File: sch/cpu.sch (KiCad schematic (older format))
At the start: 28 parts

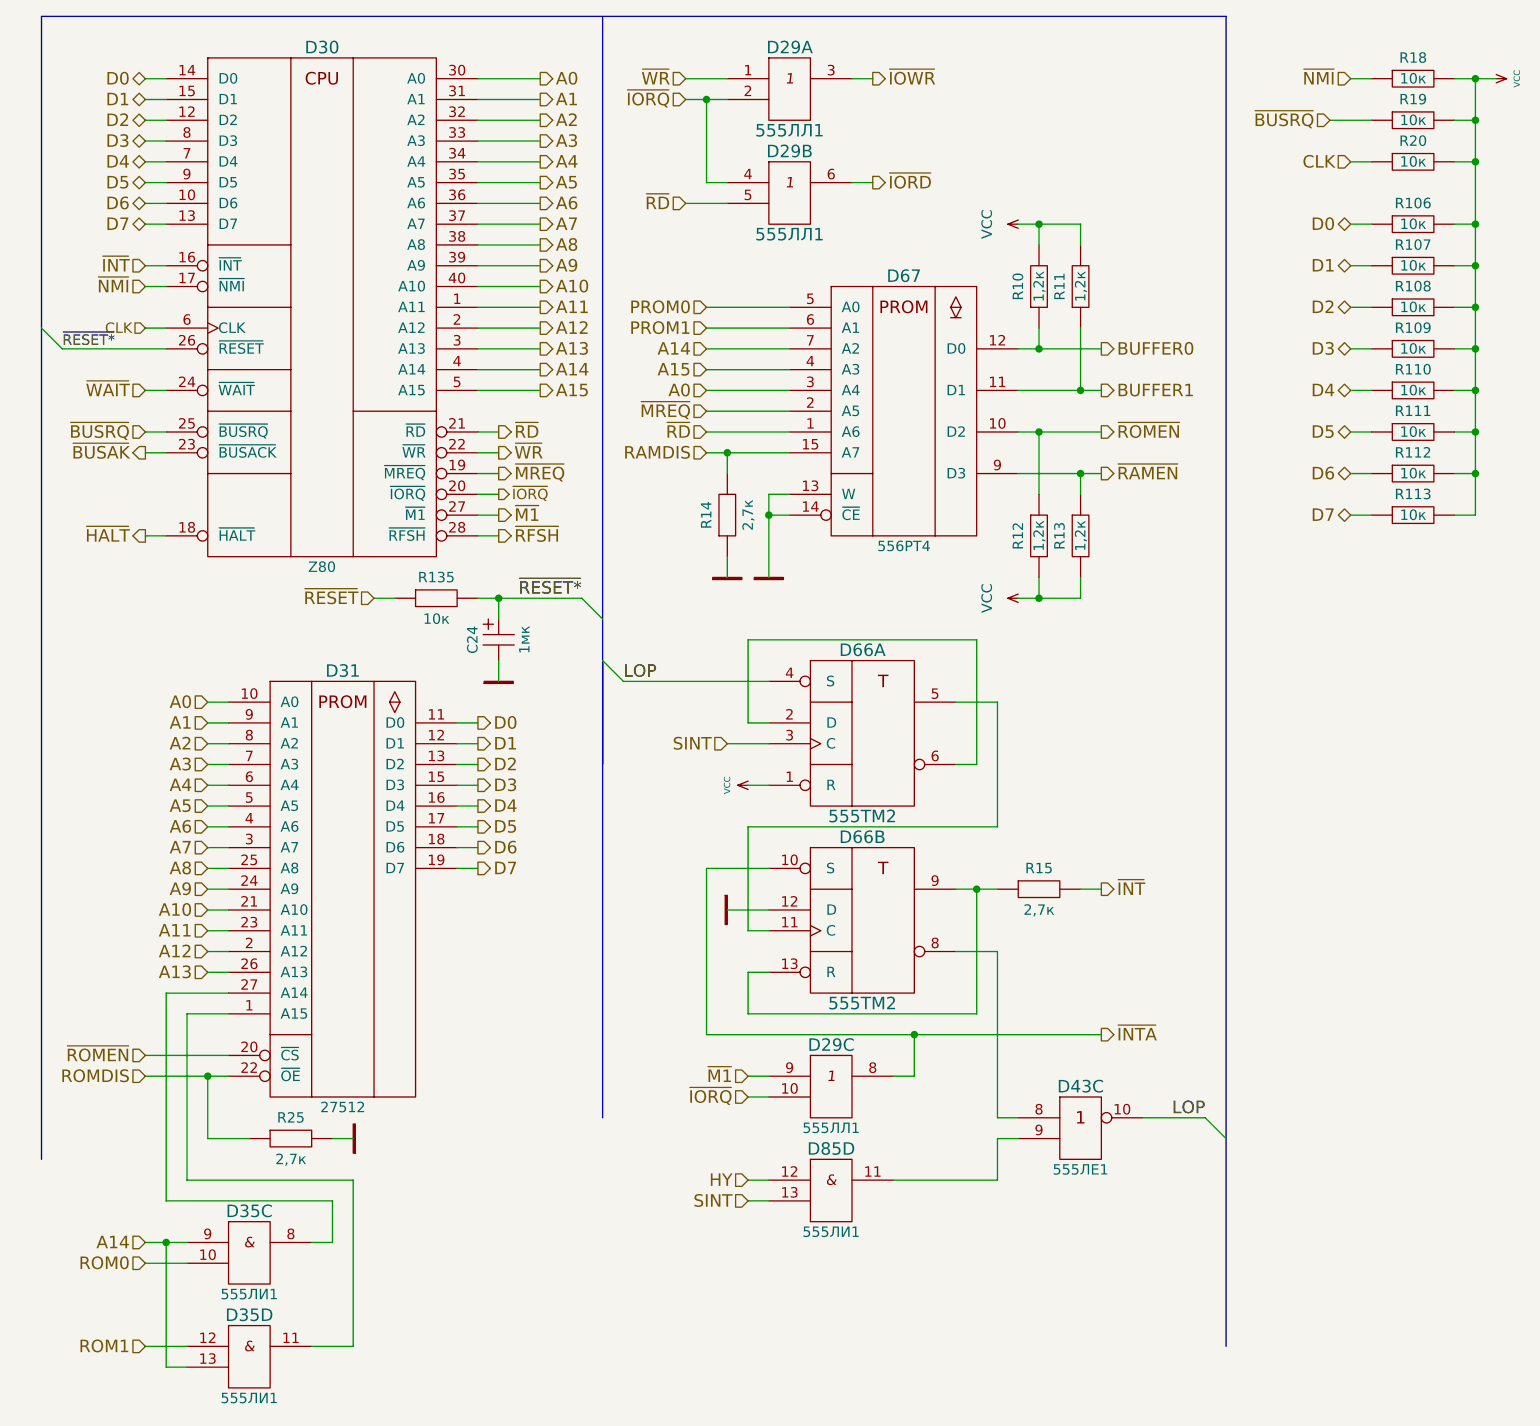
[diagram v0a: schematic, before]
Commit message: More precise version. PCB needs a lot of work.
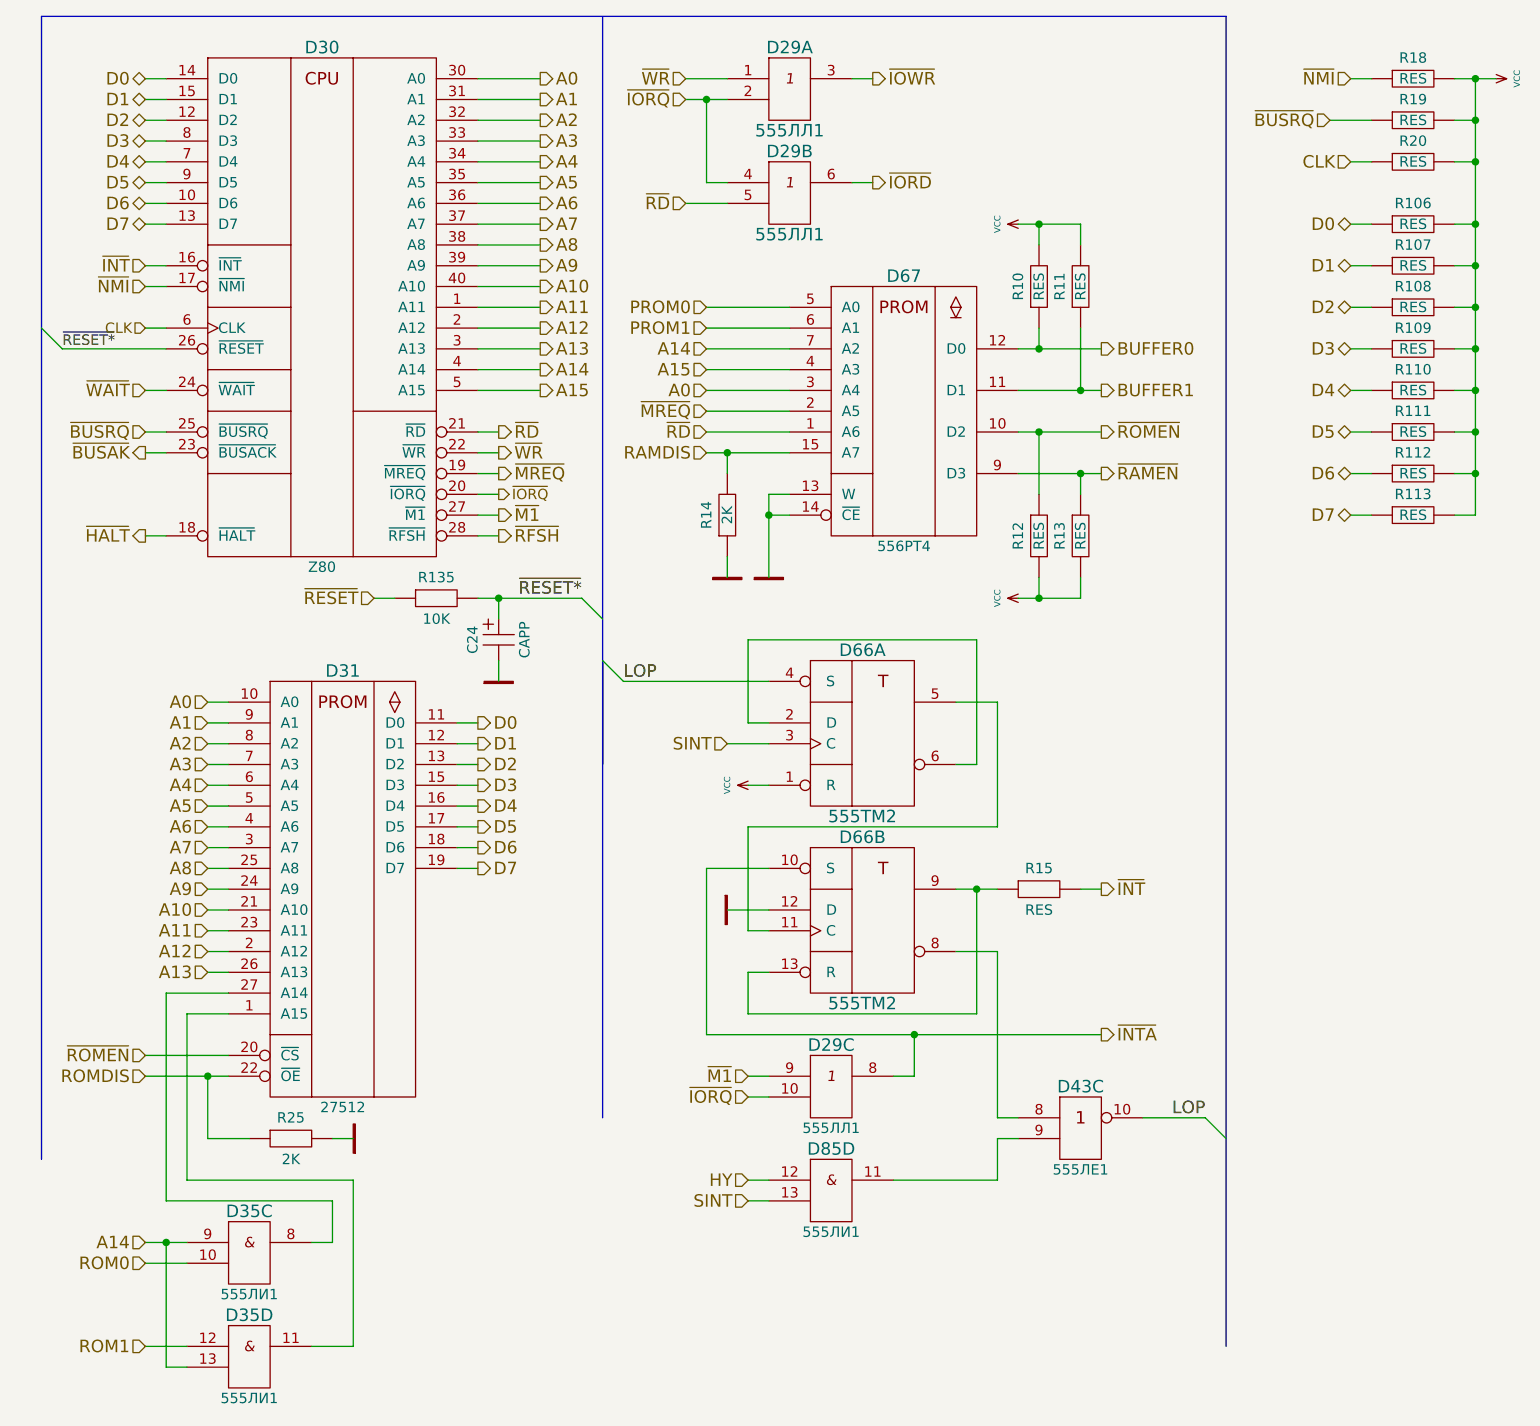
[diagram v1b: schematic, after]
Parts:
- C24: value 1мк -> CAPP
- D29, D35, D43, D66, D85: footprint MyLib:DIP-14 -> MyLib_metric:DIP-14
- D30: footprint MyLib:DIP-40 -> MyLib_metric:DIP-40
- D31: footprint MyLib:DIP-28 -> MyLib_metric:DIP-28
- D67: footprint MyLib:DIP-16 -> MyLib_metric:DIP-16
- R10, R11, R12, R13: value 1,2к -> RES; footprint MyLib:Resistor_Vertical_RM2.5mm -> MyLib_metric:Resistor_Vertical_RM2.5mm
- R106, R107, R108, R109, R110, R111, R112, R113, R18, R19, R20: value 10к -> RES; footprint MyLib:Resistor_Vertical_RM2.5mm -> MyLib_metric:Resistor_Vertical_RM2.5mm
- R135: value 10к -> 10K; footprint MyLib:Resistor_Horizontal_RM7.5mm -> MyLib_metric:Resistor_Horizontal_RM7.5mm
- R14, R25: value 2,7к -> 2K; footprint MyLib:Resistor_Horizontal_RM7.5mm -> MyLib_metric:Resistor_Horizontal_RM7.5mm
- R15: value 2,7к -> RES; footprint MyLib:Resistor_Horizontal_RM7.5mm -> MyLib_metric:Resistor_Horizontal_RM7.5mm

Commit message: IR22 and IR23 symbols updated, part values updated
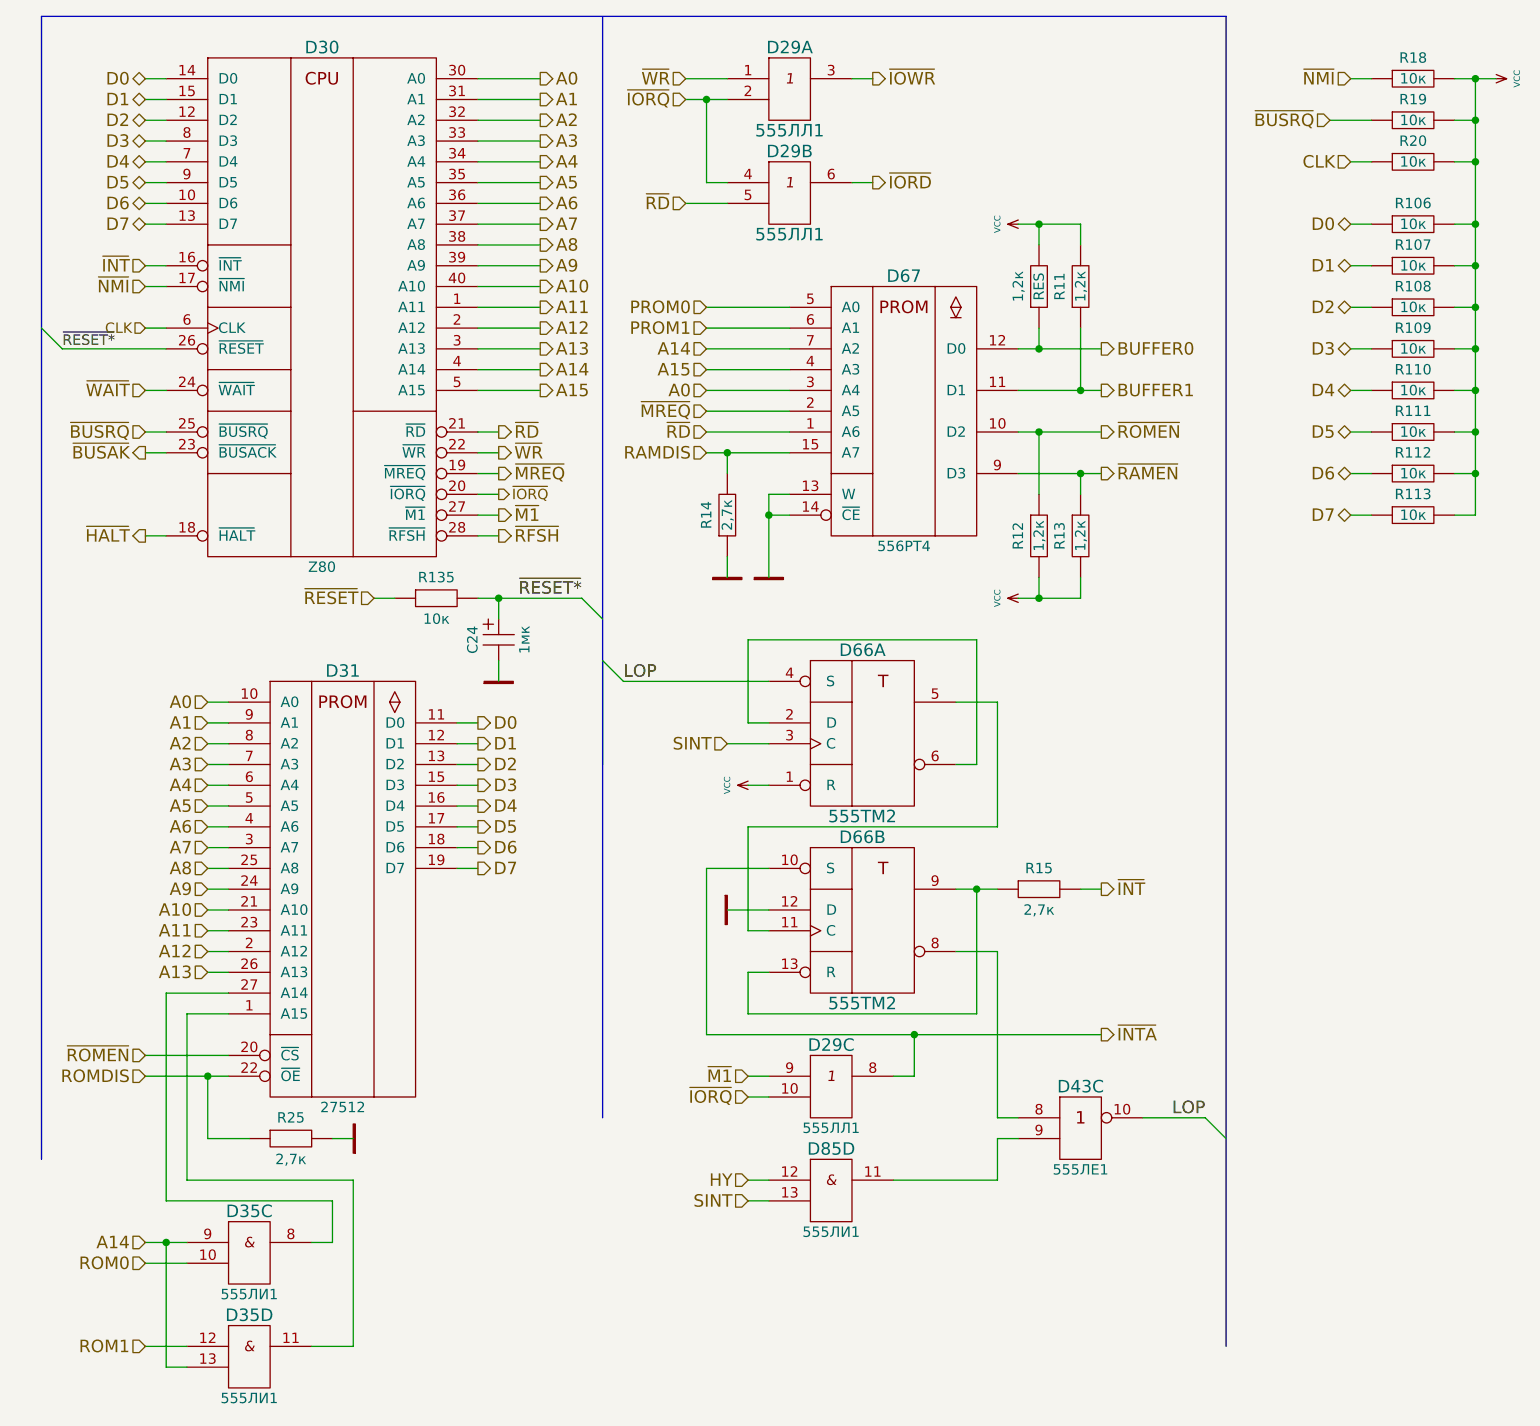
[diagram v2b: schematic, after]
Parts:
- C24: value CAPP -> 1мк
- R106, R107, R108, R109, R110, R111, R112, R113, R18, R19, R20: value RES -> 10к
- R11, R12, R13: value RES -> 1,2к
- R135: value 10K -> 10к
- R14, R25: value 2K -> 2,7к
- R15: value RES -> 2,7к
- renumbered R10 to 1,2к
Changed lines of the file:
@@
 P 1800 6000
 F 0 "R25" H 1800 6100 50  0000 C CNN
-F 1 "2K" H 1800 5900 50  0000 C CNN
+F 1 "2,7к" H 1800 5900 50  0000 C CNN
 F 2 "MyLib_metric:Resistor_Horizontal_RM7.5mm" H 1800 5950 60  0001 C CNN
 F 3 "" H 1800 5950 60  0000 C CNN
@@
 P 3900 3000
 F 0 "R14" H 3900 3100 50  0000 C CNN
-F 1 "2K" H 3900 3000 50  0000 C CNN
+F 1 "2,7к" H 3900 3000 50  0000 C CNN
 F 2 "MyLib_metric:Resistor_Horizontal_RM7.5mm" H 3900 2950 60  0001 C CNN
 F 3 "" H 3900 2950 60  0000 C CNN
@@
 	5300 2600 5700 2600
 $Comp
-L RES R10
+L RES 1,2к
 U 1 1 56901764
 P 5400 1900
-F 0 "R10" H 5400 2000 50  0000 C CNN
+F 0 "1,2к" H 5400 2000 50  0000 C CNN
 F 1 "RES" H 5400 1900 50  0000 C CNN
 F 2 "MyLib_metric:Resistor_Vertical_RM2.5mm" H 5400 1850 60  0001 C CNN
@@
 P 5600 1900
 F 0 "R11" H 5600 2000 50  0000 C CNN
-F 1 "RES" H 5600 1900 50  0000 C CNN
+F 1 "1,2к" H 5600 1900 50  0000 C CNN
 F 2 "MyLib_metric:Resistor_Vertical_RM2.5mm" H 5600 1850 60  0001 C CNN
 F 3 "" H 5600 1850 60  0000 C CNN
@@
 P 5400 3100
 F 0 "R12" H 5400 3200 50  0000 C CNN
-F 1 "RES" H 5400 3100 50  0000 C CNN
+F 1 "1,2к" H 5400 3100 50  0000 C CNN
 F 2 "MyLib_metric:Resistor_Vertical_RM2.5mm" H 5400 3050 60  0001 C CNN
 F 3 "" H 5400 3050 60  0000 C CNN
@@
 P 5600 3100
 F 0 "R13" H 5600 3200 50  0000 C CNN
-F 1 "RES" H 5600 3100 50  0000 C CNN
+F 1 "1,2к" H 5600 3100 50  0000 C CNN
 F 2 "MyLib_metric:Resistor_Vertical_RM2.5mm" H 5600 3050 60  0001 C CNN
 F 3 "" H 5600 3050 60  0000 C CNN
@@
 P 5400 4800
 F 0 "R15" H 5400 4900 50  0000 C CNN
-F 1 "RES" H 5400 4700 50  0000 C CNN
+F 1 "2,7к" H 5400 4700 50  0000 C CNN
 F 2 "MyLib_metric:Resistor_Horizontal_RM7.5mm" H 5400 4750 60  0001 C CNN
 F 3 "" H 5400 4750 60  0000 C CNN
@@
 P 7200 1600
 F 0 "R106" H 7200 1700 50  0000 C CNN
-F 1 "RES" H 7200 1600 50  0000 C CNN
+F 1 "10к" H 7200 1600 50  0000 C CNN
 F 2 "MyLib_metric:Resistor_Vertical_RM2.5mm" H 7200 1550 60  0001 C CNN
 F 3 "" H 7200 1550 60  0000 C CNN
@@
 P 7200 1800
 F 0 "R107" H 7200 1900 50  0000 C CNN
-F 1 "RES" H 7200 1800 50  0000 C CNN
+F 1 "10к" H 7200 1800 50  0000 C CNN
 F 2 "MyLib_metric:Resistor_Vertical_RM2.5mm" H 7200 1750 60  0001 C CNN
 F 3 "" H 7200 1750 60  0000 C CNN
@@
 P 7200 2000
 F 0 "R108" H 7200 2100 50  0000 C CNN
-F 1 "RES" H 7200 2000 50  0000 C CNN
+F 1 "10к" H 7200 2000 50  0000 C CNN
 F 2 "MyLib_metric:Resistor_Vertical_RM2.5mm" H 7200 1950 60  0001 C CNN
 F 3 "" H 7200 1950 60  0000 C CNN
@@
 P 7200 2200
 F 0 "R109" H 7200 2300 50  0000 C CNN
-F 1 "RES" H 7200 2200 50  0000 C CNN
+F 1 "10к" H 7200 2200 50  0000 C CNN
 F 2 "MyLib_metric:Resistor_Vertical_RM2.5mm" H 7200 2150 60  0001 C CNN
 F 3 "" H 7200 2150 60  0000 C CNN
@@
 P 7200 2400
 F 0 "R110" H 7200 2500 50  0000 C CNN
-F 1 "RES" H 7200 2400 50  0000 C CNN
+F 1 "10к" H 7200 2400 50  0000 C CNN
 F 2 "MyLib_metric:Resistor_Vertical_RM2.5mm" H 7200 2350 60  0001 C CNN
 F 3 "" H 7200 2350 60  0000 C CNN
@@
 P 7200 2600
 F 0 "R111" H 7200 2700 50  0000 C CNN
-F 1 "RES" H 7200 2600 50  0000 C CNN
+F 1 "10к" H 7200 2600 50  0000 C CNN
 F 2 "MyLib_metric:Resistor_Vertical_RM2.5mm" H 7200 2550 60  0001 C CNN
 F 3 "" H 7200 2550 60  0000 C CNN
@@
 P 7200 2800
 F 0 "R112" H 7200 2900 50  0000 C CNN
-F 1 "RES" H 7200 2800 50  0000 C CNN
+F 1 "10к" H 7200 2800 50  0000 C CNN
 F 2 "MyLib_metric:Resistor_Vertical_RM2.5mm" H 7200 2750 60  0001 C CNN
 F 3 "" H 7200 2750 60  0000 C CNN
@@
 P 7200 3000
 F 0 "R113" H 7200 3100 50  0000 C CNN
-F 1 "RES" H 7200 3000 50  0000 C CNN
+F 1 "10к" H 7200 3000 50  0000 C CNN
 F 2 "MyLib_metric:Resistor_Vertical_RM2.5mm" H 7200 2950 60  0001 C CNN
 F 3 "" H 7200 2950 60  0000 C CNN
@@
 P 7200 900
 F 0 "R18" H 7200 1000 50  0000 C CNN
-F 1 "RES" H 7200 900 50  0000 C CNN
+F 1 "10к" H 7200 900 50  0000 C CNN
 F 2 "MyLib_metric:Resistor_Vertical_RM2.5mm" H 7200 850 60  0001 C CNN
 F 3 "" H 7200 850 60  0000 C CNN
@@
 P 7200 1100
 F 0 "R19" H 7200 1200 50  0000 C CNN
-F 1 "RES" H 7200 1100 50  0000 C CNN
+F 1 "10к" H 7200 1100 50  0000 C CNN
 F 2 "MyLib_metric:Resistor_Vertical_RM2.5mm" H 7200 1050 60  0001 C CNN
 F 3 "" H 7200 1050 60  0000 C CNN
@@
 P 7200 1300
 F 0 "R20" H 7200 1400 50  0000 C CNN
-F 1 "RES" H 7200 1300 50  0000 C CNN
+F 1 "10к" H 7200 1300 50  0000 C CNN
 F 2 "MyLib_metric:Resistor_Vertical_RM2.5mm" H 7200 1250 60  0001 C CNN
 F 3 "" H 7200 1250 60  0000 C CNN
@@
 P 2500 3400
 F 0 "R135" H 2500 3500 50  0000 C CNN
-F 1 "10K" H 2500 3300 50  0000 C CNN
+F 1 "10к" H 2500 3300 50  0000 C CNN
 F 2 "MyLib_metric:Resistor_Horizontal_RM7.5mm" H 2500 3350 60  0001 C CNN
 F 3 "" H 2500 3350 60  0000 C CNN
@@
 P 2800 3600
 F 0 "C24" H 2800 3725 50  0000 C CNN
-F 1 "CAPP" H 2800 3475 50  0000 C CNN
+F 1 "1мк" H 2800 3475 50  0000 C CNN
 F 2 "Capacitors_ThroughHole:C_Radial_D5_L6_P2.5" H 2800 3550 60  0001 C CNN
 F 3 "" H 2800 3550 60  0000 C CNN

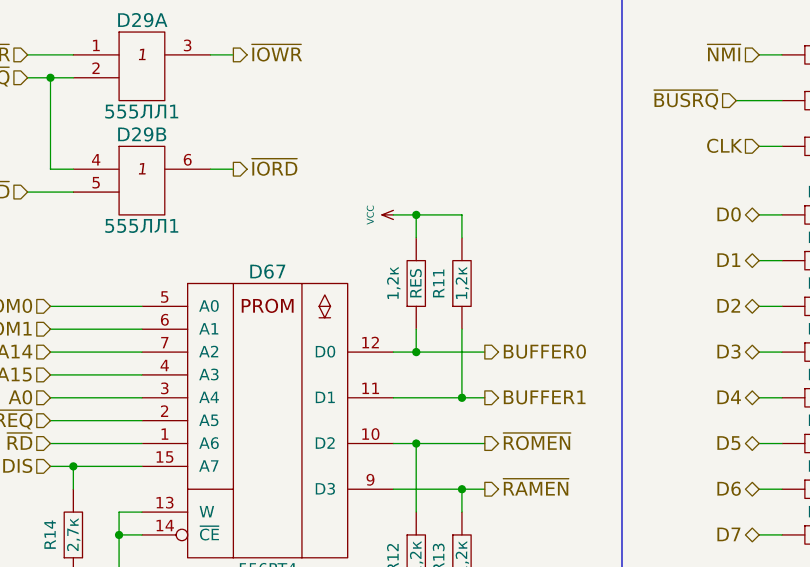
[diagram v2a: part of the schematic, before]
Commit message: Board fully redrawn
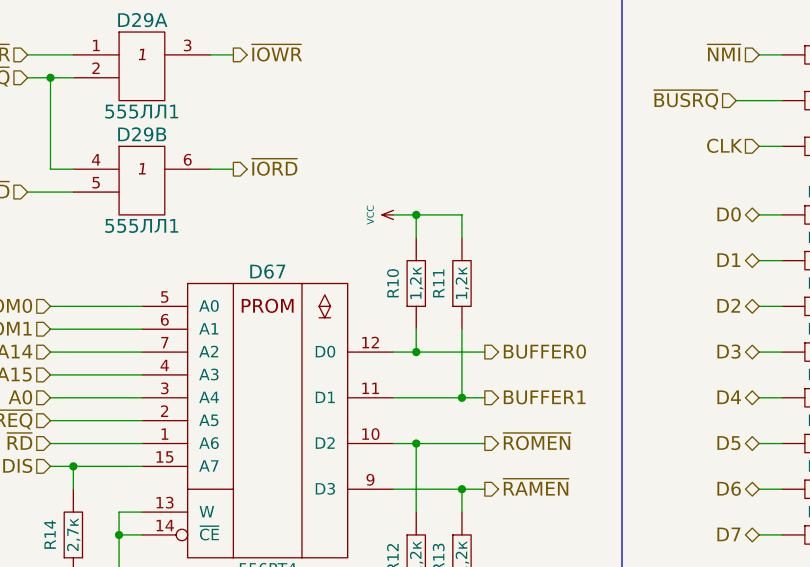
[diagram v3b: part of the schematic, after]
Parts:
- R10: renamed from 1,2к; value RES -> 1,2к
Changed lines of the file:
@@
 	5300 2600 5700 2600
 $Comp
-L RES 1,2к
+L RES R10
 U 1 1 56901764
 P 5400 1900
-F 0 "1,2к" H 5400 2000 50  0000 C CNN
-F 1 "RES" H 5400 1900 50  0000 C CNN
+F 0 "R10" H 5400 2000 50  0000 C CNN
+F 1 "1,2к" H 5400 1900 50  0000 C CNN
 F 2 "MyLib_metric:Resistor_Vertical_RM2.5mm" H 5400 1850 60  0001 C CNN
 F 3 "" H 5400 1850 60  0000 C CNN
